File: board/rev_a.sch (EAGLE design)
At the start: 1 part, among them IC1 STM32F303CB

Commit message: Working on schematic
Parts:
- added BUF: MCP6002, Seeed-IC:AMPLIFIER-LMV358IDGKR(MSOP8)
- added C1, C4: 10nF 6v, rcl:C-USC0805
- added C2, C3: 4.7uF 6v, rcl:C-USC0805
- added CLK: ASE 8MHz, crystal:ASE
- added D1: BAT54S, diode:BAT54S
- added D2: (no value), diode:DIODE-SOD323-R
- added J1: CORTEX_DEBUG_PTH, SparkFun-Connectors:CORTEX_DEBUG_PTH
- added J2: USB_MINI-B_SMT, SparkFun-Connectors:USB_MINI-B_SMT
- added LDO1, LDO2: LDK120M33R, SparkFun-IC-Power:V_REG_MIC52053.3V
- added R1, R2: 47k, rcl:R-US_R0805
- added R3, R4: 22R, rcl:R-US_R0805
- renumbered IC1 to MCU
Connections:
- new net CLK_IN: CLK.OUT, MCUPORTD/OSC.PD0/OSC<=
- new net COMP1_IN: MCUPORTA_L.PA1
- new net COMP2_IN: MCUPORTA_L.PA7
- new net COMP6_IN: MCUPORTB_H.PB11
- new net DAC1: BUFG$2.+IN1, MCUPORTA_L.PA4
- new net DAC1_BUF: BUFG$2.-IN1, BUFG$2.OUT1, R2.1
- new net DAC2: BUFG$1.+IN2, MCUPORTA_L.PA5
- new net DAC2_BUF: BUFG$1.-IN2, BUFG$1.OUT2
- new net GND: BUFG$2.GND, C1.2, C2.2, C3.2, C4.2, CLK.GND, D1.A1, J1.GND@3, J1.GND@5, J1.GNDDTCT, J2.GND, J2.SHIELD, LDO1.GND, LDO2.GND, MCUAN_POWER.VSSA, MCUPOWER.VSS_1, MCUPOWER.VSS_2, MCUPOWER.VSS_3
- new net N$1: C1.1, LDO2.BP
- new net N$2: C4.1, CLK.VDD
- new net N$3: J2.D+, R4.2
- new net N$4: J2.D-, R3.2
- new net N$5: D2.A, J2.VBUS
- new net NRST: J1.!RESET, MCURESET.NRST
- new net OPA1_IN: D1.C1A2, MCUPORTA_L.PA3, R1.2
- new net OPA1_OUT: MCUPORTA_L.PA2
- new net OPA2_IN: MCUPORTB_H.PB14
- new net OPA2_OUT: MCUPORTA_L.PA6
- new net OPA3_IN: MCUPORTB_L.PB0
- new net OPA3_OUT: MCUPORTB_L.PB1
- new net OPA4_IN: MCUPORTB_H.PB13
- new net OPA4_OUT: MCUPORTB_H.PB12
- new net SPI_MISO: MCUPORTB_L.PB4
- new net SPI_MOSI: MCUPORTB_L.PB5
- new net SPI_NSS: MCUPORTA_H.PA15
- new net SPI_SCK: MCUPORTB_L.PB3
- new net SWD_CLK: J1.SWDCLK/TCK, MCUPORTA_H.PA14
- new net SWD_IO: J1.SWDIO/TMS, MCUPORTA_H.PA13
- new net TR1_OUT: MCUPORTA_L.PA0
- new net TR2_OUT: MCUPORTB_H.PB9
- new net TR3_OUT: MCUPORTA_H.PA10
- new net USB_DM: MCUPORTA_H.PA11, R3.1
- new net USB_DP: MCUPORTA_H.PA12, R4.1
- new net VCC: D2.C, LDO1.EN, LDO1.IN, LDO2.EN, LDO2.IN
- new net VDD: C3.1, J1.VCC, LDO1.OUT, MCUAN_POWER.VBAT, MCUPOWER.VDD_1, MCUPOWER.VDD_2, MCUPOWER.VDD_3
- new net VDDA: BUFG$2.+V, C2.1, D1.C2, LDO2.OUT, MCUAN_POWER.VDDA
- new net VR1+: R1.1
- new net VR1-: R2.2

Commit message: Updated VR inputs
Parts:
- added C5, C6, C7: 10nF 6v, rcl:C-USC0805
- added C8: 100nF 50v, rcl:C-USC0805
- added D3, D4, D5: BAT54S, diode:BAT54S
- added JP1: JUMPER-SMT_3_2-NC_PASTE_SILK, SparkFun-Jumpers:JUMPER-SMT_3_2-NC_PASTE_SILK
- added R10, R11, R13, R5, R7, R8: 1k, rcl:R-US_R0805
- added R12: 470k, rcl:R-US_R0805
- added R6, R9: 47k, rcl:R-US_R0805
- R2: value 47k -> 1k
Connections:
- removed net COMP1_IN: MCUPORTA_L.PA1
- removed net COMP2_IN: MCUPORTA_L.PA7
- removed net COMP6_IN: MCUPORTB_H.PB11
- removed net OPA1_IN: D1.C1A2, MCUPORTA_L.PA3, R1.2
- removed net OPA2_IN: MCUPORTB_H.PB14
- removed net OPA3_IN: MCUPORTB_L.PB0
- removed net OPA4_IN: MCUPORTB_H.PB13
- new net KNK_BIAS: R13.2
- new net KNK_IN: C8.1
- new net N$6: C8.2, R12.2
- new net N$7: CLK.OUT, JP1.3
- new net N$9: JP1.2, MCUPORTD/OSC.PD0/OSC<=
- new net OPA1/COMP1_INP: C5.2, D1.C1A2, MCUPORTA_L.PA1, MCUPORTA_L.PA3, R1.2, R5.1
- new net OPA2_INP: D5.C1A2, MCUPORTB_H.PB14, R12.1
- new net OPA3/COMP2_INP: C6.2, D3.C1A2, MCUPORTA_L.PA7, MCUPORTB_L.PB0, R6.2, R8.1
- new net OPA4/COMP6_INP: C7.2, D4.C1A2, MCUPORTB_H.PB11, MCUPORTB_H.PB13, R11.1, R9.2
- new net VR2+: R6.1
- new net VR2-: R7.2
- new net VR3+: R9.1
- new net VR3-: R10.2
- net CLK_IN: now also JP1.1; no longer CLK.OUT, MCUPORTD/OSC.PD0/OSC<=
- net DAC1_BUF: now also C5.1, C6.1, C7.1, R10.1, R11.2, R5.2, R7.1, R8.2
- net GND: now also D3.A1, D4.A1, D5.A1
- net VDDA: now also D3.C2, D4.C2, D5.C2, R13.1
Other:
- note added: "1/47 divider gives us about +/-80V range before clamping"

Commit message: Cleaning schematic and mcu file
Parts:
- added J3, J4, J5, J6: (no value), SparkFun-Connectors:CONN_02LOCK
- added R14: 10k, rcl:R-US_R0805
- C8: value 100nF 50v -> 10nF 6v
- R12: value 470k -> 10k
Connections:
- removed net N$6: C8.2, R12.2
- new net INTERRUPT: MCUPORTC.PC14
- new net SAMPLE: MCUPORTC.PC13
- net DAC1_BUF: now also C8.1, R13.1, R14.2
- net KNK_BIAS: now also J6.1
- net KNK_IN: now also J6.2, R12.1; no longer C8.1
- net OPA2_INP: now also C8.2, R12.2, R14.1; no longer R12.1
- net VDDA: no longer R13.1
- net VR1+: now also J3.2
- net VR1-: now also J3.1
- net VR2+: now also J4.2
- net VR2-: now also J4.1
- net VR3+: now also J5.2
- net VR3-: now also J5.1
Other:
- note added: "1/(1+1) divider to get max range of +/-6V"
- note added: "1/(47+1) divider gives us about +/-80V range before clamping"
- note added: "Decoupling"
- note added: "Power supply"
- note removed: "1/47 divider gives us about +/-80V range before clamping"
- moved on the sheet: C7, C8, D4, D5, R10, R11, R12, R13, R2, R9

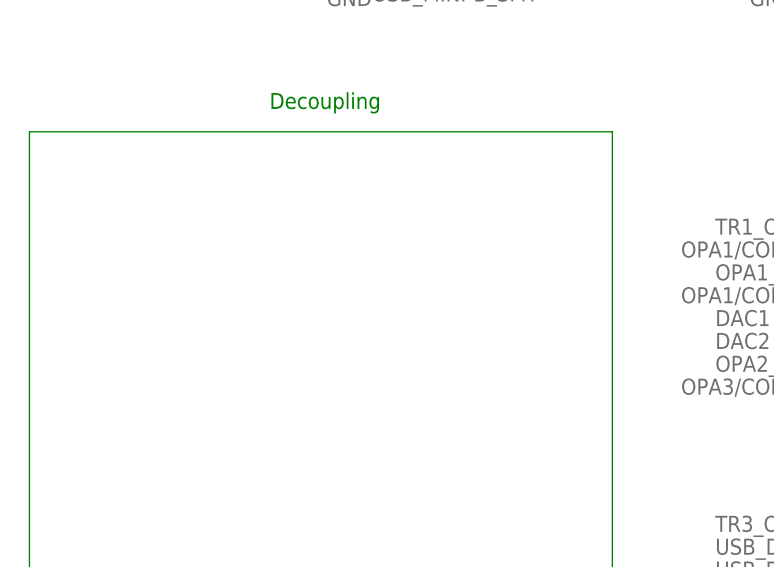
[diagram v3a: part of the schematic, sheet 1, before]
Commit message: [board] Adding decoupling caps
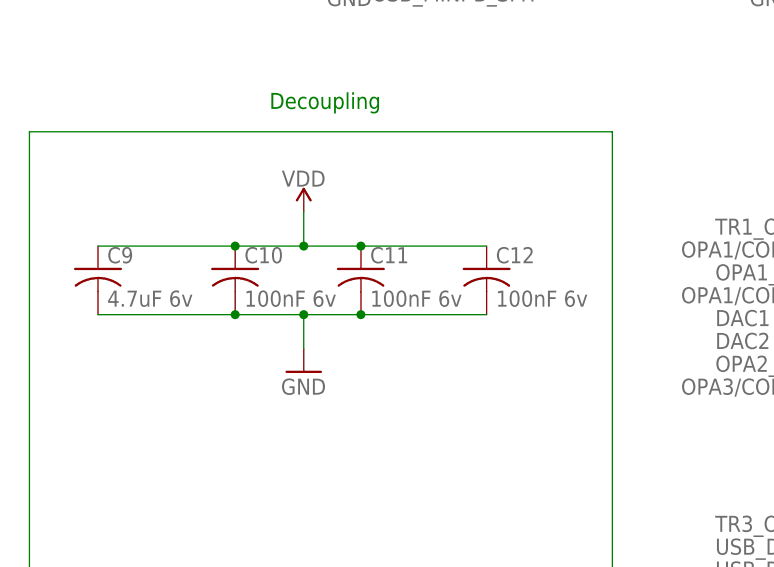
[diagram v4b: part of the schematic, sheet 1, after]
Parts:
- added C10, C11, C12: 100nF 6v, rcl:C-USC0805
- added C9: 4.7uF 6v, rcl:C-USC0805
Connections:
- net GND: now also C10.2, C11.2, C12.2, C9.2
- net VDD: now also C10.1, C11.1, C12.1, C9.1
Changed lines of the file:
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@@
 <part name="R14" library="rcl" library_urn="urn:adsk.eagle:library:334" deviceset="R-US_" device="R0805" package3d_urn="urn:adsk.eagle:package:23553/2" value="10k"/>
 <part name="C8" library="rcl" library_urn="urn:adsk.eagle:library:334" deviceset="C-US" device="C0805" package3d_urn="urn:adsk.eagle:package:23617/2" value="10nF 6v"/>
+<part name="C9" library="rcl" library_urn="urn:adsk.eagle:library:334" deviceset="C-US" device="C0805" package3d_urn="urn:adsk.eagle:package:23617/2" value="4.7uF 6v"/>
+<part name="C10" library="rcl" library_urn="urn:adsk.eagle:library:334" deviceset="C-US" device="C0805" package3d_urn="urn:adsk.eagle:package:23617/2" value="100nF 6v"/>
+<part name="C11" library="rcl" library_urn="urn:adsk.eagle:library:334" deviceset="C-US" device="C0805" package3d_urn="urn:adsk.eagle:package:23617/2" value="100nF 6v"/>
+<part name="C12" library="rcl" library_urn="urn:adsk.eagle:library:334" deviceset="C-US" device="C0805" package3d_urn="urn:adsk.eagle:package:23617/2" value="100nF 6v"/>
+<part name="SUPPLY6" library="SparkFun-PowerSymbols" library_urn="urn:adsk.eagle:library:530" deviceset="VDD" device=""/>
+<part name="GND16" library="supply1" library_urn="urn:adsk.eagle:library:371" deviceset="GND" device=""/>
 </parts>
 <sheets>
@@
 <attribute name="VALUE" x="153.67" y="88.519" size="1.778" layer="96" font="vector" align="top-left"/>
 </instance>
+<instance part="C9" gate="G$1" x="15.24" y="140.97" smashed="yes">
+<attribute name="NAME" x="16.256" y="141.605" size="1.778" layer="95"/>
+<attribute name="VALUE" x="16.256" y="136.779" size="1.778" layer="96"/>
+</instance>
+<instance part="C10" gate="G$1" x="30.48" y="140.97" smashed="yes">
+<attribute name="NAME" x="31.496" y="141.605" size="1.778" layer="95"/>
+<attribute name="VALUE" x="31.496" y="136.779" size="1.778" layer="96"/>
+</instance>
+<instance part="C11" gate="G$1" x="44.45" y="140.97" smashed="yes">
+<attribute name="NAME" x="45.466" y="141.605" size="1.778" layer="95"/>
+<attribute name="VALUE" x="45.466" y="136.779" size="1.778" layer="96"/>
+</instance>
+<instance part="C12" gate="G$1" x="58.42" y="140.97" smashed="yes">
+<attribute name="NAME" x="59.436" y="141.605" size="1.778" layer="95"/>
+<attribute name="VALUE" x="59.436" y="136.779" size="1.778" layer="96"/>
+</instance>
+<instance part="SUPPLY6" gate="VDD" x="38.1" y="147.32" smashed="yes">
+<attribute name="VALUE" x="38.1" y="150.114" size="1.778" layer="96" align="bottom-center"/>
+</instance>
+<instance part="GND16" gate="1" x="38.1" y="129.54" smashed="yes">
+<attribute name="VALUE" x="35.56" y="127" size="1.778" layer="96"/>
+</instance>
 </instances>
 <busses>
@@
 <wire x1="102.87" y1="175.26" x2="90.17" y2="175.26" width="0.1524" layer="91"/>
 </segment>
+<segment>
+<pinref part="C9" gate="G$1" pin="2"/>
+<pinref part="C10" gate="G$1" pin="2"/>
+<wire x1="15.24" y1="135.89" x2="30.48" y2="135.89" width="0.1524" layer="91"/>
+<pinref part="C11" gate="G$1" pin="2"/>
+<wire x1="30.48" y1="135.89" x2="38.1" y2="135.89" width="0.1524" layer="91"/>
+<junction x="30.48" y="135.89"/>
+<pinref part="C12" gate="G$1" pin="2"/>
+<wire x1="38.1" y1="135.89" x2="44.45" y2="135.89" width="0.1524" layer="91"/>
+<wire x1="44.45" y1="135.89" x2="58.42" y2="135.89" width="0.1524" layer="91"/>
+<junction x="44.45" y="135.89"/>
+<pinref part="GND16" gate="1" pin="GND"/>
+<wire x1="38.1" y1="132.08" x2="38.1" y2="135.89" width="0.1524" layer="91"/>
+<junction x="38.1" y="135.89"/>
+</segment>
 </net>
 <net name="TR1_OUT" class="0">
@@
 <wire x1="102.87" y1="185.42" x2="102.87" y2="191.77" width="0.1524" layer="91"/>
 </segment>
-</net>
+<segment>
+<pinref part="C9" gate="G$1" pin="1"/>
+<pinref part="C10" gate="G$1" pin="1"/>
+<wire x1="15.24" y1="143.51" x2="30.48" y2="143.51" width="0.1524" layer="91"/>
+<pinref part="C11" gate="G$1" pin="1"/>
+<wire x1="30.48" y1="143.51" x2="38.1" y2="143.51" width="0.1524" layer="91"/>
+<junction x="30.48" y="143.51"/>
+<pinref part="C12" gate="G$1" pin="1"/>
+<wire x1="38.1" y1="143.51" x2="44.45" y2="143.51" width="0.1524" layer="91"/>
+<wire x1="44.45" y1="143.51" x2="58.42" y2="143.51" width="0.1524" layer="91"/>
+<junction x="44.45" y="143.51"/>
+<pinref part="SUPPLY6" gate="VDD" pin="VDD"/>
+<wire x1="38.1" y1="143.51" x2="38.1" y2="147.32" width="0.1524" layer="91"/>
+<junction x="38.1" y="143.51"/>
+</segment>
+</net>
